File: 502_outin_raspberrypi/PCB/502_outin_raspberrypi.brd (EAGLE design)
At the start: 85 x 56 mm, 19 parts

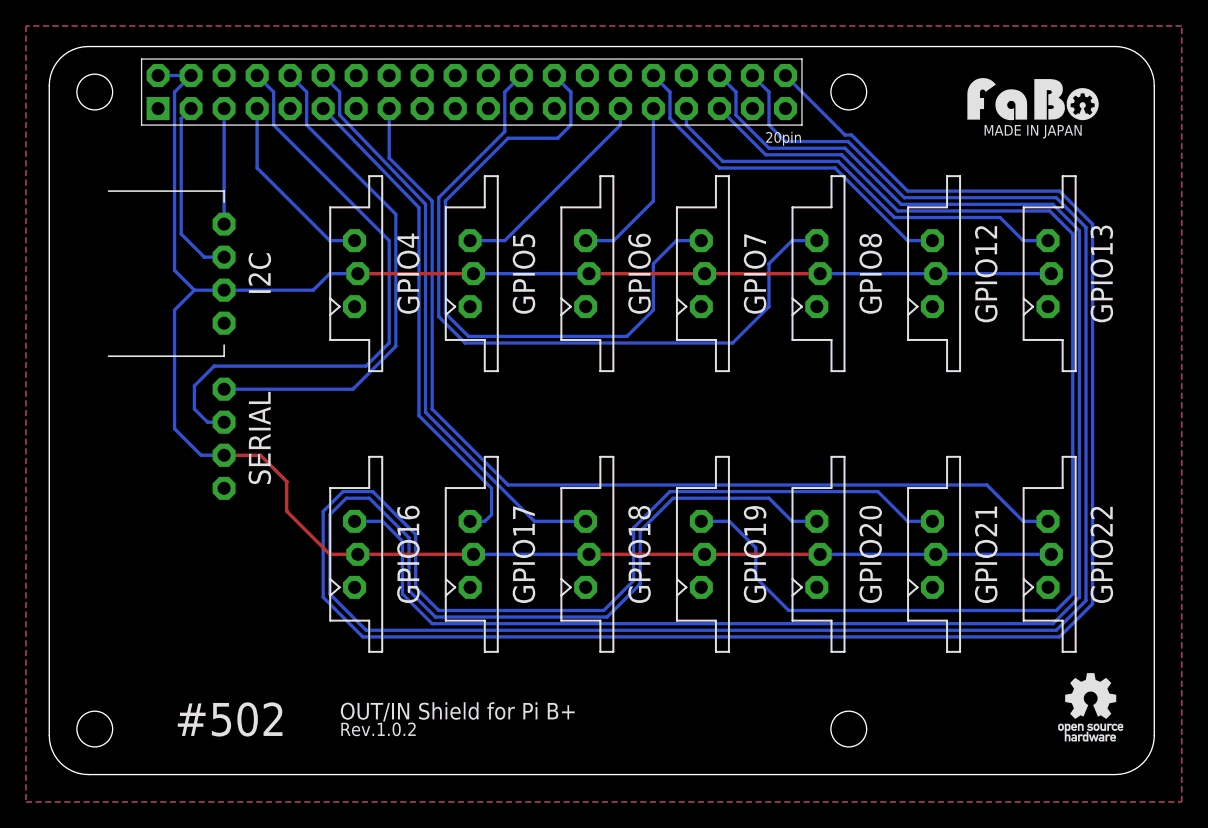
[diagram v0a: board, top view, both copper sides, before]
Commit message: change connector
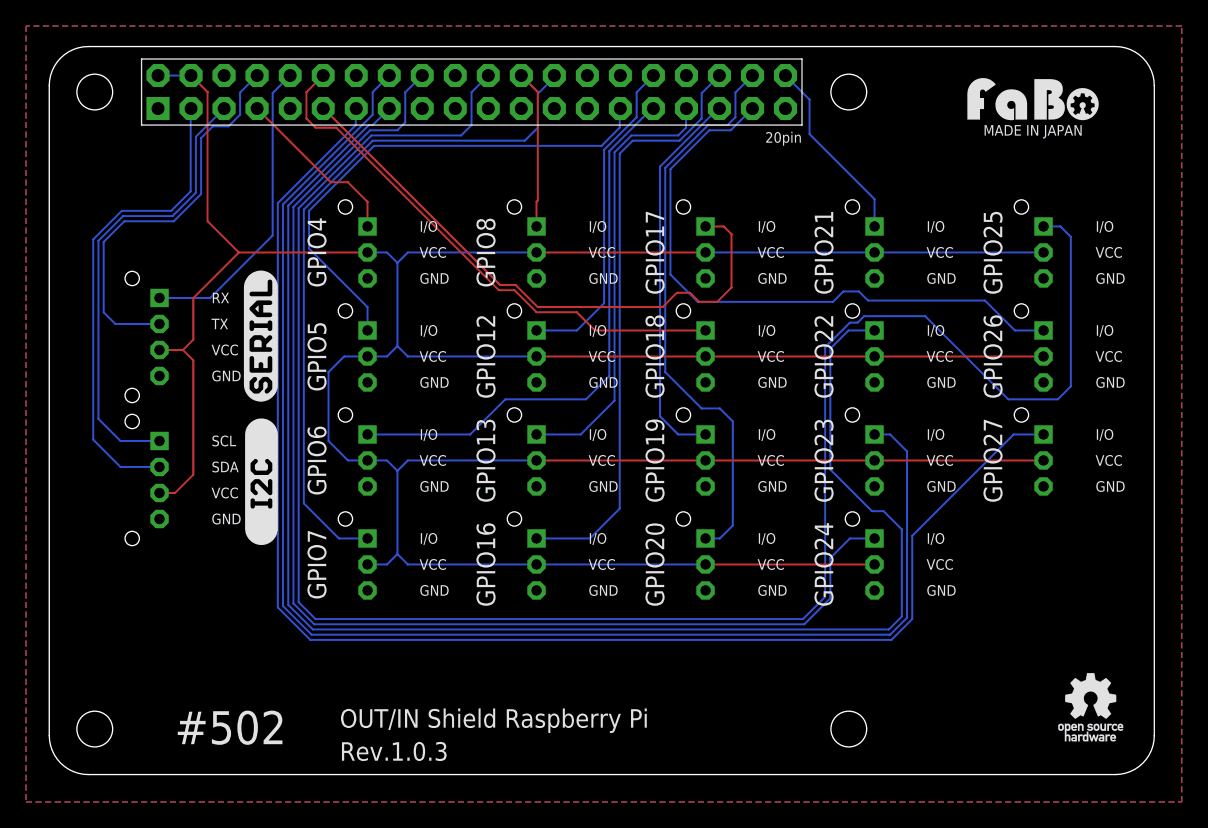
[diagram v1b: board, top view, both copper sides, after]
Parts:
- added GPIO23, GPIO24, GPIO25, GPIO26, GPIO27: (no value), FaBo-Template:FABO_BRICK_3PIN_B03B-PASK-1
- added U$2: (no value), FaBo-etc:LOGO_SILK_I2C
- added U$3: (no value), FaBo-etc:LOGO_SILK_SERIAL2
- GPIO12, GPIO13, GPIO16, GPIO17, GPIO18, GPIO19, GPIO20, GPIO21, GPIO22, GPIO4, GPIO5, GPIO6, GPIO7, GPIO8: device FaBo-Template:FABO_BRICK_3PIN_HEADER -> FaBo-Template:FABO_BRICK_3PIN_B03B-PASK-1
- I2C: device FaBo-Template:FABO_BRICK_I2C_CONNECTOR -> FaBo-Template:FABO_BRICK_I2C_S04B-PASK-2
- SERIAL: device FaBo-Template:FABO_BRICK_SERIAL_CONNECTOR -> FaBo-Template:FABO_BRICK_SERIAL_S04B-PASK-2
- moved GPIO13 42.0 mm to (38.0, 25.0)
- moved GPIO7 34.1 mm to (25.0, 17.0)
- moved GPIO12 31.2 mm to (38.0, 33.0)
- moved GPIO17 29.4 mm to (51.0, 41.0)
- moved GPIO21 23.7 mm to (64.0, 41.0)
- moved GPIO6 22.2 mm to (25.0, 25.0)
- moved GPIO8 21.8 mm to (38.0, 41.0)
- moved GPIO22 20.3 mm to (64.0, 33.0)
- moved GPIO18 17.7 mm to (51.0, 33.0)
- moved I2C 16.6 mm to (9.00, 23.5)
- moved GPIO16 13.9 mm to (38.0, 17.0)
- moved GPIO5 10.2 mm to (25.0, 33.0)
- moved SERIAL 9.27 mm to (9.00, 34.5)
- moved GPIO20 8.72 mm to (51.0, 17.0)
- moved GPIO19 7.22 mm to (51.0, 25.0)
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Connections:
- net 5V: now also GPIO23.VCC, GPIO24.VCC, GPIO25.VCC, GPIO26.VCC, GPIO27.VCC
- net GND: now also GPIO23.GND, GPIO24.GND, GPIO25.GND, GPIO26.GND, GPIO27.GND
- net GPIO23: now also GPIO23.I/O
- net GPIO24: now also GPIO24.I/O
- net GPIO25: now also GPIO25.I/O
- net GPIO26: now also GPIO26.I/O
- net GPIO27: now also GPIO27.I/O
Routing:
- net GPIO21: track 186.4 -> 14.4 mm
- net GPIO25: track 0.00 -> 148.4 mm
- net GPIO20: track 178.1 -> 43.8 mm
- net GPIO27: track 0.00 -> 111.1 mm
- net GPIO23: track 0.00 -> 109.5 mm
- net 5V: track 170.7 -> 274.6 mm
- net GPIO24: track 0.00 -> 95.9 mm
- net GPIO16: track 124.1 -> 45.9 mm
- net GPIO19: track 92.1 -> 29.7 mm
- net GPIO26: track 0.00 -> 47.5 mm
- net GPIO8: track 56.3 -> 12.2 mm
- net GPIO22: track 75.4 -> 117.4 mm
- net GPIO6: track 13.6 -> 42.5 mm
- net SCL: track 8.89 -> 35.5 mm
- net SDA: track 14.0 -> 36.8 mm
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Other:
- board text added: "GND"
- board text added: "I/O"
- board text added: "OUT/IN Shield Raspberry Pi"
- board text added: "RX"
- board text added: "Rev.1.0.3"
- board text added: "SCL"
- board text added: "SDA"
- board text added: "TX"
- board text added: "VCC"
- board text removed: "OUT/IN Shield for Pi B+"
- board text removed: "Rev.1.0.2"

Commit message: change layout
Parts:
- removed GPIO12, GPIO13, GPIO16, GPIO19, GPIO20, GPIO21, GPIO26, GPIO5, GPIO6, GPIO7, GPIO8: (no value), FaBo-Template:FABO_BRICK_3PIN_B03B-PASK-1
- removed I2C: (no value), FaBo-Template:FABO_BRICK_I2C_S04B-PASK-2
- added A0, A1, A2, A3, A4, A5, A6, A7: (no value), FaBo-Template:FABO_BRICK_3PIN_B03B-PASK-1
- added I2C1, I2C2: (no value), FaBo-Template:FABO_BRICK_I2C_B04B-PASK-1
- added IC1: (no value), FaBo-ADC:MICROCHIP-MCP3008
- added U$5: (no value), FaBo-etc:LOGO_SILK_I2C
- moved GPIO27 41.5 mm to (38.5, 40.5)
- moved GPIO25 39.4 mm to (38.5, 32.5)
- moved GPIO22 39.2 mm to (25.5, 40.5)
- moved GPIO17 30.4 mm to (25.5, 24.5)
- moved GPIO23 26.9 mm to (38.5, 16.5)
- moved GPIO24 26.6 mm to (38.5, 24.5)
- moved GPIO18 25.5 mm to (25.5, 32.5)
- moved GPIO4 24.5 mm to (25.5, 16.5)
- moved U$3 7.00 mm to (18.0, 36.5)
- moved SERIAL 7.00 mm to (9.00, 41.5)
- moved U$2 5.64 mm to (15.5, 23.5)
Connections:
- removed net GPIO12: GPIO12.I/O, U1.32
- removed net GPIO13: GPIO13.I/O, U1.33
- removed net GPIO16: GPIO16.I/O, U1.36
- removed net GPIO19: GPIO19.I/O, U1.35
- removed net GPIO20: GPIO20.I/O, U1.38
- removed net GPIO21: GPIO21.I/O, U1.40
- removed net GPIO26: GPIO26.I/O, U1.37
- removed net GPIO5: GPIO5.I/O, U1.29
- removed net GPIO6: GPIO6.I/O, U1.31
- removed net GPIO7: GPIO7.I/O, U1.26
- removed net GPIO8: GPIO8.I/O, U1.24
- new net CE0: IC1.10, U1.24
- new net CH0: A0.I/O, IC1.1
- new net CH1: A1.I/O, IC1.2
- new net CH2: A2.I/O, IC1.3
- new net CH3: A3.I/O, IC1.4
- new net CH4: A4.I/O, IC1.5
- new net CH5: A5.I/O, IC1.6
- new net CH6: A6.I/O, IC1.7
- new net CH7: A7.I/O, IC1.8
- new net MISO: IC1.12, U1.21
- new net MOSI: IC1.11, U1.19
- new net SCLK: IC1.13, U1.23
- net 5V: now also A0.VCC, A1.VCC, A2.VCC, A3.VCC, A4.VCC, A5.VCC, A6.VCC, A7.VCC, I2C1.VCC, I2C2.VCC, IC1.15, IC1.16; no longer GPIO12.VCC, GPIO13.VCC, GPIO16.VCC, GPIO19.VCC, GPIO20.VCC, GPIO21.VCC, GPIO26.VCC, GPIO5.VCC, GPIO6.VCC, GPIO7.VCC, GPIO8.VCC, I2C.VCC
- net GND: now also A0.GND, A1.GND, A2.GND, A3.GND, A4.GND, A5.GND, A6.GND, A7.GND, I2C1.GND, I2C2.GND, IC1.14, IC1.9; no longer GPIO12.GND, GPIO13.GND, GPIO16.GND, GPIO19.GND, GPIO20.GND, GPIO21.GND, GPIO26.GND, GPIO5.GND, GPIO6.GND, GPIO7.GND, GPIO8.GND, I2C.GND
- net SCL: now also I2C1.SCL, I2C2.SCL; no longer I2C.SCL
- net SDA: now also I2C1.SDA, I2C2.SDA; no longer I2C.SDA
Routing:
- net GPIO25: track 148.4 -> 23.0 mm
- net GPIO22: track 117.4 -> 10.3 mm
- net CH3: track 0.00 -> 66.9 mm
- net GPIO23: track 109.5 -> 43.3 mm
- net MOSI: track 0.00 -> 63.5 mm
- net MISO: track 0.00 -> 63.0 mm
- net GPIO24: track 95.9 -> 33.0 mm
- net SCLK: track 0.00 -> 62.3 mm
- net CH2: track 0.00 -> 58.4 mm
- net CE0: track 0.00 -> 57.4 mm, vias 0 -> 1
- net GPIO7: track 53.8 -> 0.00 mm
- net CH1: track 0.00 -> 49.9 mm
- net CH7: track 0.00 -> 48.4 mm
- net GPIO26: track 47.5 -> 0.00 mm
- net GPIO16: track 45.9 -> 0.00 mm
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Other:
- board text added: "ANALOG"
- board text added: "GPIO"
- board text added: "Rev.1.0.4"
- board text removed: "20pin"
- board text removed: "Rev.1.0.3"

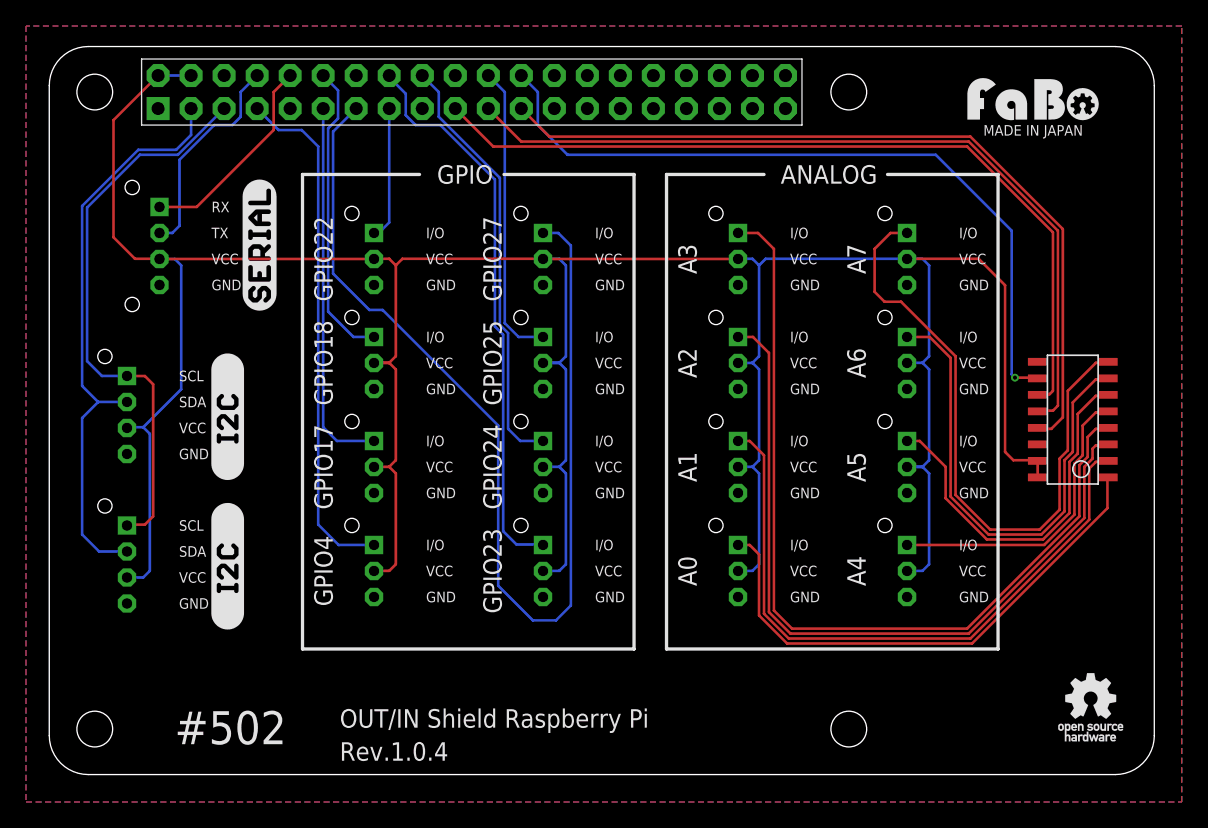
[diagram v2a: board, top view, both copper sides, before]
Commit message: change connector
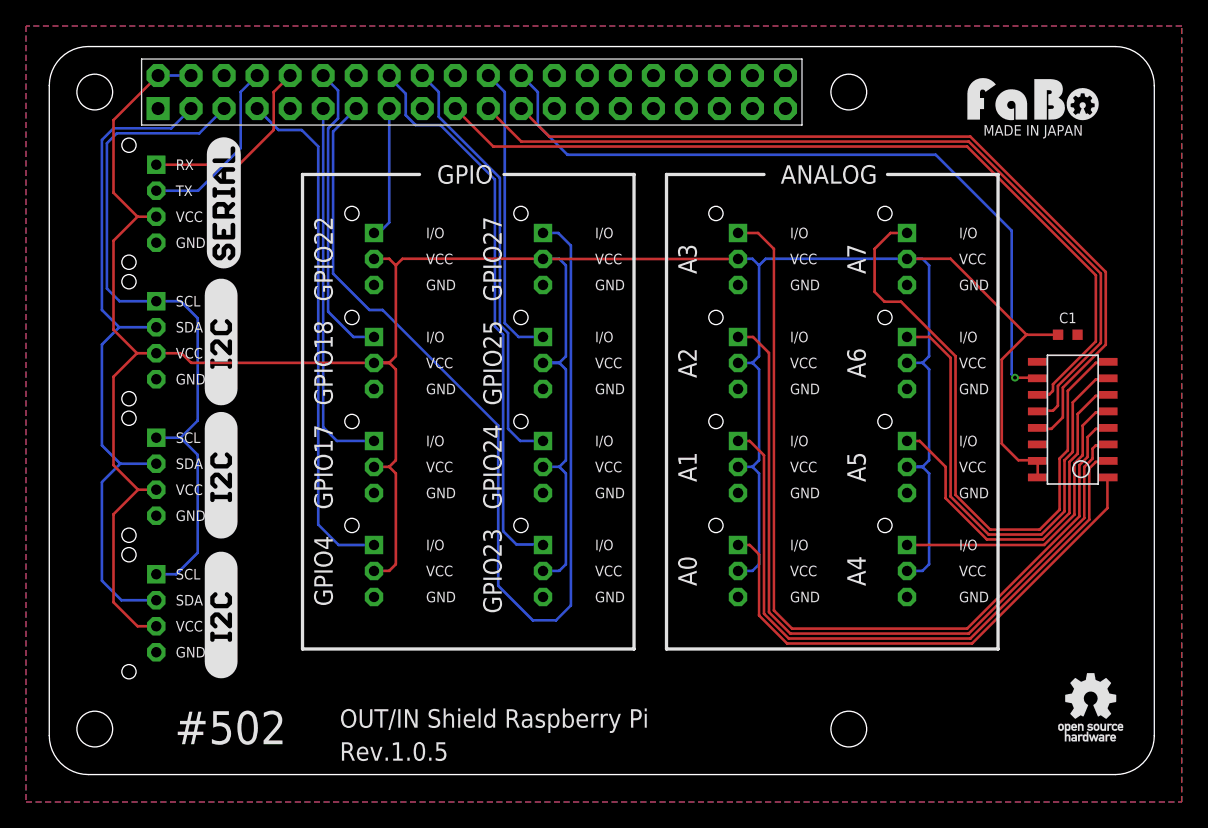
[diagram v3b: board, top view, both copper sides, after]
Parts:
- added C1: 0.1uF, FaBo-Capacitor:0603
- added I2C3: (no value), FaBo-Template:FABO_BRICK_I2C_S04B-PASK-2
- added U$6: (no value), FaBo-etc:LOGO_SILK_I2C
- I2C1, I2C2: device FaBo-Template:FABO_BRICK_I2C_B04B-PASK-1 -> FaBo-Template:FABO_BRICK_I2C_S04B-PASK-2
- moved I2C2 7.12 mm to (8.75, 23.8)
- moved I2C1 6.17 mm to (8.75, 34.2)
- moved U$2 4.53 mm to (15.0, 19.0)
- moved U$3 4.26 mm to (15.2, 39.8)
- moved U$5 3.78 mm to (15.0, 8.25)
- moved SERIAL 3.26 mm to (8.75, 44.8)
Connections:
- net 5V: now also C1.2, I2C3.VCC
- net GND: now also C1.1, I2C3.GND
- net SCL: now also I2C3.SCL
- net SDA: now also I2C3.SDA
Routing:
- net SCL: track 43.8 -> 54.1 mm
- net 5V: track 254.2 -> 264.1 mm
- net SDA: track 45.2 -> 54.5 mm
- net MISO: track 63.0 -> 65.7 mm
- net MOSI: track 63.5 -> 66.2 mm
- net SCLK: track 62.3 -> 65.0 mm
- net TX: track 16.6 -> 14.0 mm
- net RX: track 15.9 -> 14.9 mm
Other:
- board text added: "Rev.1.0.5"
- board text removed: "Rev.1.0.4"

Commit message: change connector
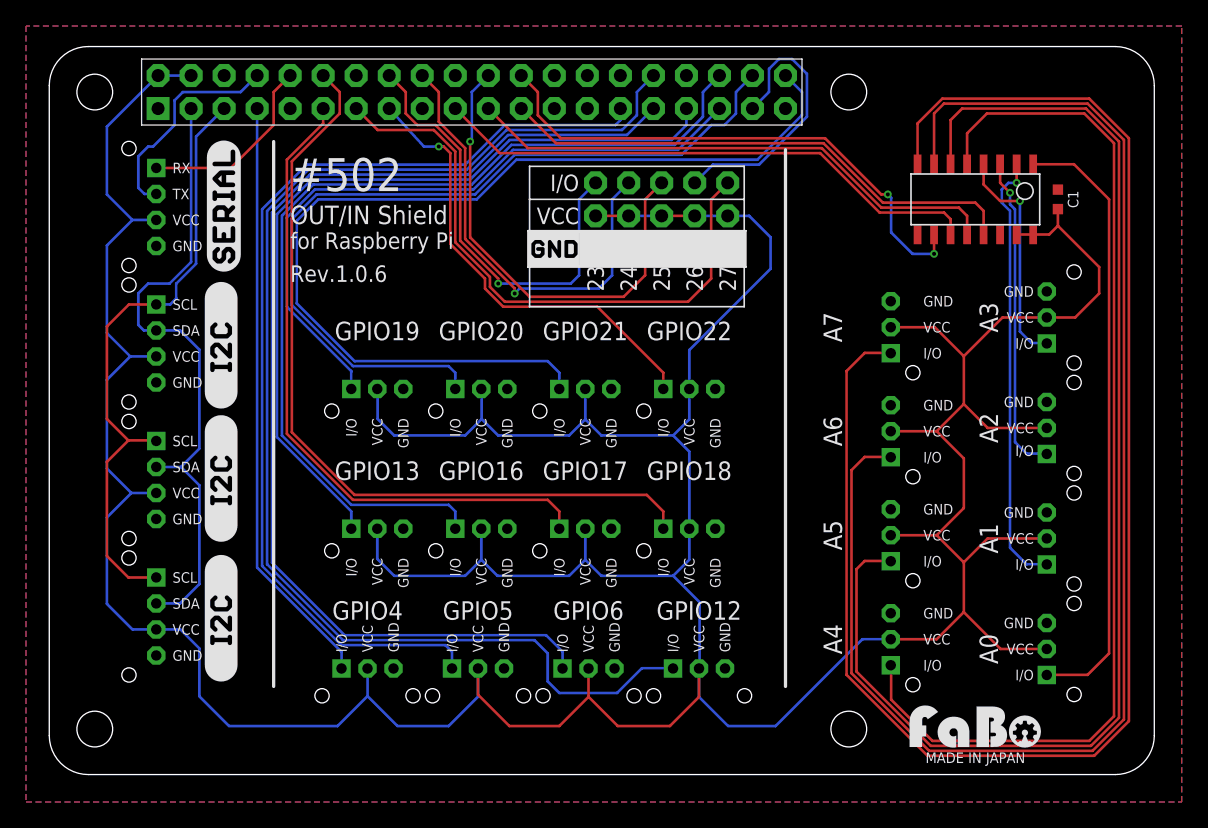
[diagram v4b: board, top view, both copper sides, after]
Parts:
- removed GPIO23, GPIO24, GPIO25, GPIO27: (no value), FaBo-Template:FABO_BRICK_3PIN_B03B-PASK-1
- added GPIO12, GPIO5, GPIO6: (no value), FaBo-Template:FABO_BRICK_3PIN_S03B-PASK-2
- added GPIO13, GPIO16, GPIO19, GPIO20, GPIO21: (no value), FaBo-Template:FABO_BRICK_3PIN_B03B-PASK-1
- added GPIO23S, GPIO24S, GPIO25S, GPIO26S, GPIO27S: (no value), FaBo-Template:FABO_BRICK_3PIN_HEADER
- added U$7: (no value), FaBo-etc:LOGO_SILK_GND
- A0, A1, A2, A3, GPIO4: device FaBo-Template:FABO_BRICK_3PIN_B03B-PASK-1 -> FaBo-Template:FABO_BRICK_3PIN_S03B-PASK-2
- U$4: device FaBo-etc:LOGO_OSHW_T_MS -> FaBo-etc:LOGO_OSHW_T_MS_BOTTOM
- moved U$14 48.5 mm to (71.8, 2.54)
- moved GPIO18 27.4 mm to (49.8, 19.8), turned to 180 degrees
- moved GPIO22 26.2 mm to (49.8, 30.5), turned to 180 degrees
- moved A0 24.5 mm to (77.2, 10.5), turned to 270 degrees
- moved A1 24.4 mm to (77.2, 19.0), turned to 270 degrees
- moved A2 24.3 mm to (77.2, 27.5), turned to 270 degrees
- moved A3 24.2 mm to (77.2, 36.0), turned to 270 degrees
- moved U$4 20.6 mm to (80.6, 27.3), turned to 90 degrees
- moved IC1 18.5 mm to (71.8, 45.1), turned to 180 degrees
- moved GPIO17 16.9 mm to (41.8, 19.8), turned to 180 degrees
- moved C1 10.4 mm to (78.1, 45.1), turned to 270 degrees
- moved GPIO4 7.52 mm to (25.0, 9.00), turned to 180 degrees
- moved A4 5.40 mm to (65.2, 11.2), turned to 270 degrees
- moved A5 5.40 mm to (65.2, 19.2), turned to 270 degrees
- moved A6 5.40 mm to (65.2, 27.2), turned to 270 degrees
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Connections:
- new net GPIO12: GPIO12.I/O, U1.32
- new net GPIO13: GPIO13.I/O, U1.33
- new net GPIO16: GPIO16.I/O, U1.36
- new net GPIO19: GPIO19.I/O, U1.35
- new net GPIO20: GPIO20.I/O, U1.38
- new net GPIO21: GPIO21.I/O, U1.40
- new net GPIO26: GPIO26S.I/O, U1.37
- new net GPIO5: GPIO5.I/O, U1.29
- new net GPIO6: GPIO6.I/O, U1.31
- net 5V: now also GPIO12.VCC, GPIO13.VCC, GPIO16.VCC, GPIO19.VCC, GPIO20.VCC, GPIO21.VCC, GPIO23S.VCC, GPIO24S.VCC, GPIO25S.VCC, GPIO26S.VCC, GPIO27S.VCC, GPIO5.VCC, GPIO6.VCC; no longer GPIO23.VCC, GPIO24.VCC, GPIO25.VCC, GPIO27.VCC
- net GND: now also GPIO12.GND, GPIO13.GND, GPIO16.GND, GPIO19.GND, GPIO20.GND, GPIO21.GND, GPIO23S.GND, GPIO24S.GND, GPIO25S.GND, GPIO26S.GND, GPIO27S.GND, GPIO5.GND, GPIO6.GND; no longer GPIO23.GND, GPIO24.GND, GPIO25.GND, GPIO27.GND
- net GPIO23: now also GPIO23S.I/O; no longer GPIO23.I/O
- net GPIO24: now also GPIO24S.I/O; no longer GPIO24.I/O
- net GPIO25: now also GPIO25S.I/O; no longer GPIO25.I/O
- net GPIO27: now also GPIO27S.I/O; no longer GPIO27.I/O
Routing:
- net GPIO12: track 0.00 -> 99.6 mm
- net 5V: track 264.1 -> 350.6 mm
- net GPIO6: track 0.00 -> 86.1 mm
- net GPIO5: track 0.00 -> 77.3 mm
- net GPIO21: track 0.00 -> 75.8 mm
- net GPIO16: track 0.00 -> 73.2 mm
- net CH7: track 48.4 -> 119.0 mm
- net CH6: track 37.5 -> 108.1 mm
- net CH5: track 28.7 -> 96.3 mm
- net GPIO20: track 0.00 -> 63.6 mm
- net GPIO13: track 0.00 -> 62.2 mm
- net CH4: track 23.4 -> 81.2 mm
- net GPIO19: track 0.00 -> 52.0 mm
- net CH3: track 66.9 -> 17.4 mm, vias 0 -> 1
- net GPIO18: track 23.3 -> 61.9 mm
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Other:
- board text added: "23"
- board text added: "24"
- board text added: "25"
- board text added: "26"
- board text added: "27"
- board text added: "OUT/IN Shield"
- board text added: "Rev.1.0.6"
- board text added: "for Raspberry Pi"
- board text removed: "ANALOG"
- board text removed: "GPIO"
- board text removed: "OUT/IN Shield Raspberry Pi"
- board text removed: "Rev.1.0.5"
